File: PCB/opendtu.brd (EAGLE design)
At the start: 104.1 x 54 mm, 13 parts, among them M1 DISPLAY-OLED-128X64-I2CNH, M3 NRF24L01-PA-EXT, X1 MCV1,5/2G

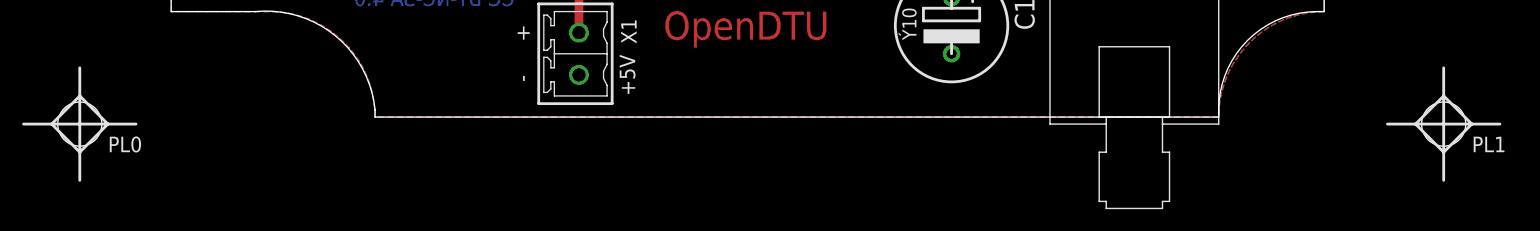
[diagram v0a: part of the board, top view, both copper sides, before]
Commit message: Board
Passlöcher vom Board entfernt. Werden zur Produktion nicht benötig. Passlöcher nur fürs Sieb & Meyer Fräsefile benötig. (für das Bohrmuster).
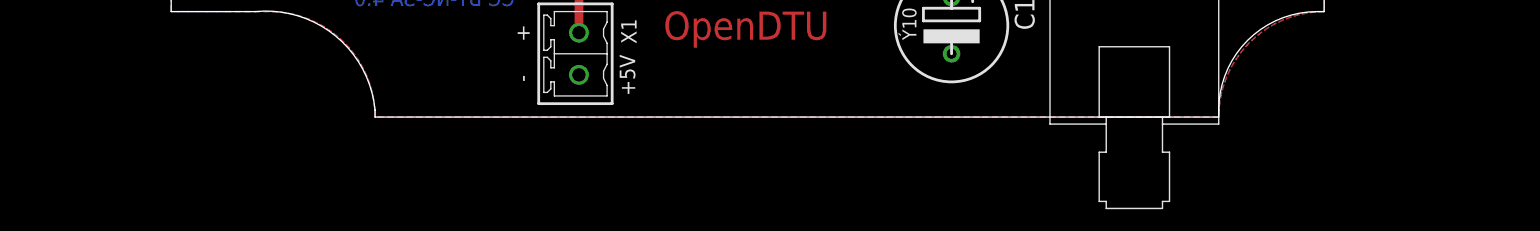
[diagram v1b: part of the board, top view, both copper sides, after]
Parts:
- removed PL0, PL1: (no value), 3PASSIVE:PASSLO2
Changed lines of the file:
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@@
 <element name="C1" library="5elko" package="EB10D" value="470uF" x="71.12" y="8.89" rot="R270"/>
 <element name="X1" library="STECKER" package="MCV1,5/2" value="MCV1,5/2G" x="37.465" y="8.255" rot="R270"/>
-<element name="PL0" library="3PASSIVE" package="PASSLO2" value="" x="-7.62" y="0"/>
-<element name="PL1" library="3PASSIVE" package="PASSLO2" value="" x="115.57" y="0"/>
 </elements>
 <signals>
